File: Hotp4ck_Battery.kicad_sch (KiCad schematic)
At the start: 23 parts, among them J3 Conn_01x02_MountingPin, Q1 2N7002, SW43 PWR, U2 BQ24075, U3 MAX17048

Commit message: Fixed position & etc..
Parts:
- LED2: value orange -> Yellow; footprint LED_SMD:LED_0402_1005Metric -> LED_SMD:LED_0603_1608Metric
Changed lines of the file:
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@@
       (effects (font (size 1.27 1.27)) (justify right))
     )
-    (property "Value" "orange" (at 86.36 71.12 90)
+    (property "Value" "Yellow" (at 86.36 71.12 90)
       (effects (font (size 1.27 1.27)) (justify right))
     )
-    (property "Footprint" "LED_SMD:LED_0402_1005Metric" (at 93.98 74.93 90)
+    (property "Footprint" "LED_SMD:LED_0603_1608Metric" (at 93.98 74.93 90)
       (effects (font (size 1.27 1.27)) hide)
     )

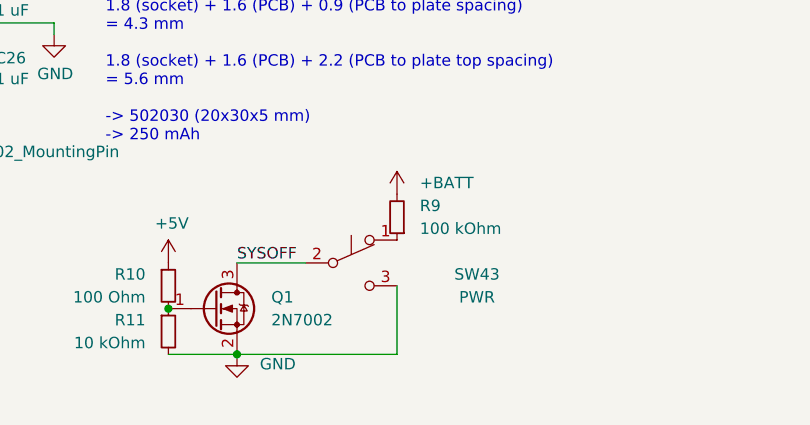
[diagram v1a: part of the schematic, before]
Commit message: Add Switch Mount pin symbol
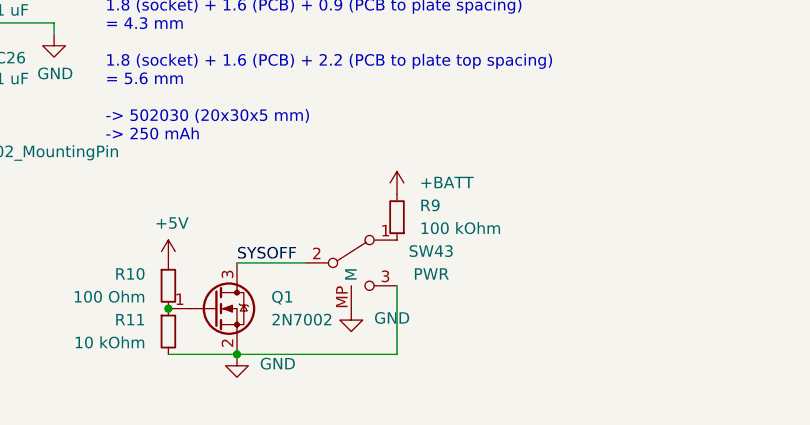
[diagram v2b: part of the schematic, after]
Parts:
- SW43: symbol Switch:SW_Push_SPDT -> marbastlib-various:SW_SPDT_mountpin
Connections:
- net GND: now also SW43.MP (M)
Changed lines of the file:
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@@
     )
   )
-  (symbol (lib_id "Switch:SW_Push_SPDT") (at 157.48 104.14 0) (unit 1)
-    (in_bom yes) (on_board yes) (dnp no)
-    (property "Reference" "SW43" (at 171.45 105.41 0)
-      (effects (font (size 1.27 1.27)))
-    )
-    (property "Value" "PWR" (at 171.45 107.95 0)
-      (effects (font (size 1.27 1.27)))
-    )
-    (property "Footprint" "marbastlib-various:SW_MSK12C02-HB" (at 157.48 104.14 0)
-      (effects (font (size 1.27 1.27)) hide)
-    )
-    (property "Datasheet" "~" (at 157.48 104.14 0)
+  (symbol (lib_id "marbastlib-various:SW_SPDT_mountpin") (at 158.75 104.14 0) (unit 1)
+    (in_bom yes) (on_board yes) (dnp no)
+    (property "Reference" "SW43" (at 166.37 102.87 0)
+      (effects (font (size 1.27 1.27)))
+    )
+    (property "Value" "PWR" (at 166.37 105.41 0)
+      (effects (font (size 1.27 1.27)))
+    )
+    (property "Footprint" "marbastlib-various:SW_MSK12C02-HB" (at 158.75 104.14 0)
+      (effects (font (size 1.27 1.27)) hide)
+    )
+    (property "Datasheet" "~" (at 158.75 104.14 0)
       (effects (font (size 1.27 1.27)) hide)
     )
@@
     (pin "2")
     (pin "3")
+    (pin "MP")
     (instances
       (project "osprey_rev_a"
@@
         )
       )
+    )
+  )
+  (symbol (lib_id "power:GND") (at 157.48 109.22 0) (unit 1)
+    (in_bom yes) (on_board yes) (dnp no) (fields_autoplaced)
+    (property "Reference" "#PWR027" (at 157.48 115.57 0)
+      (effects (font (size 1.27 1.27)) hide)
+    )
+    (property "Value" "GND" (at 160.02 110.2994 0)
+      (effects (font (size 1.27 1.27)) (justify left))
+    )
+    (property "Footprint" "" (at 157.48 109.22 0)
+      (effects (font (size 1.27 1.27)) hide)
+    )
+    (property "Datasheet" "" (at 157.48 109.22 0)
+      (effects (font (size 1.27 1.27)) hide)
+    )
+    (pin "1")
+    (instances
+      (project "osprey_rev_a"
+        (path "/86a516b3-939b-48ee-9a25-d0111c577d06/e12a0b82-f794-4b5e-b657-628292a2530a"
+          (reference "#PWR027") (unit 1)
+        )
+      )
+      (project "Hotp4ck60"
+        (path "/a57939d7-40ce-4436-8014-db245ef7f3c5"
+          (reference "#PWR023") (unit 1)
+        )
+        (path "/a57939d7-40ce-4436-8014-db245ef7f3c5/18c06ada-111b-4ec0-9dc0-78c3052676b0"
+          (reference "#PWR031") (unit 1)
+        )
+      )
+      (project "designguide-schematic"
+        (path "/c2a65ddb-3915-4293-98a9-444287fe2a3d"
+          (reference "#PWR023") (unit 1)
+        )
+      )

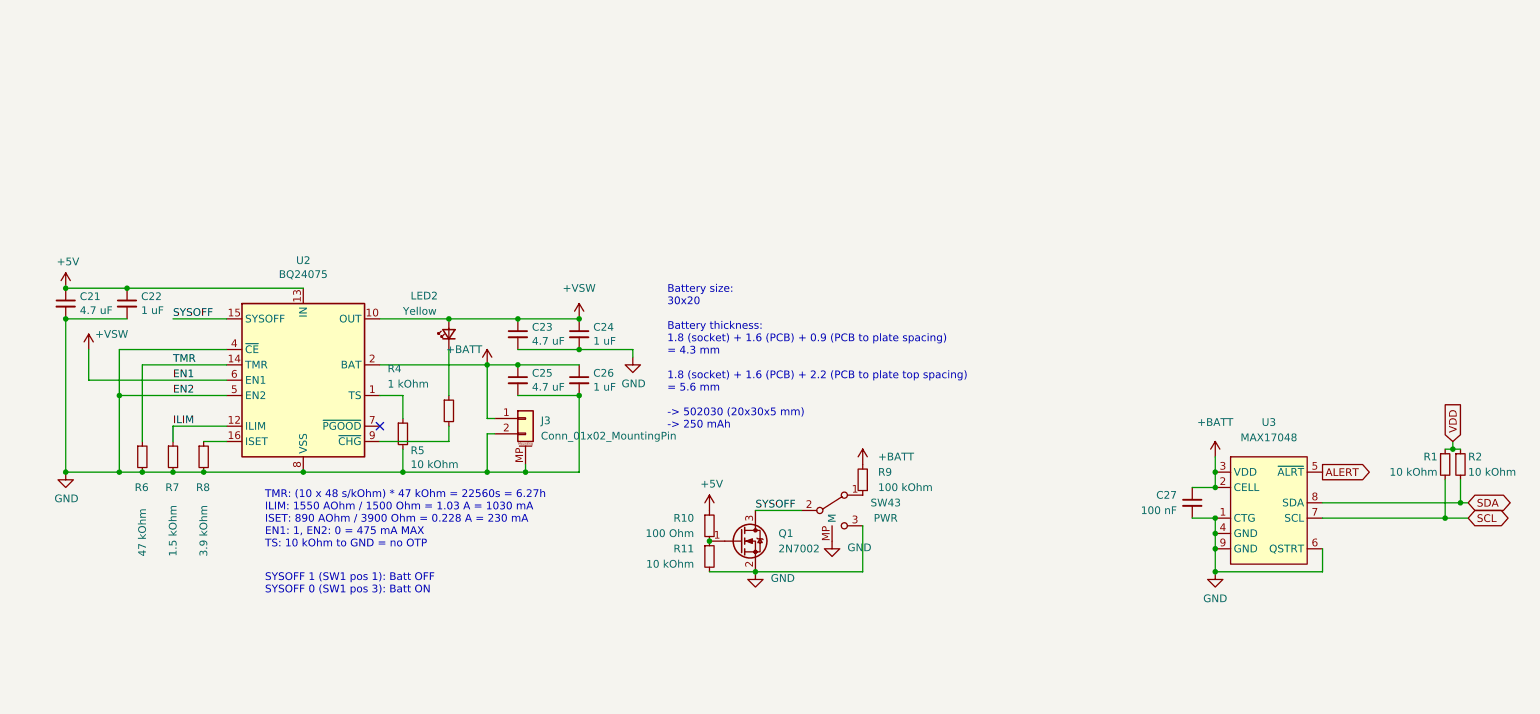
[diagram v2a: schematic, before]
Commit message: update schematic
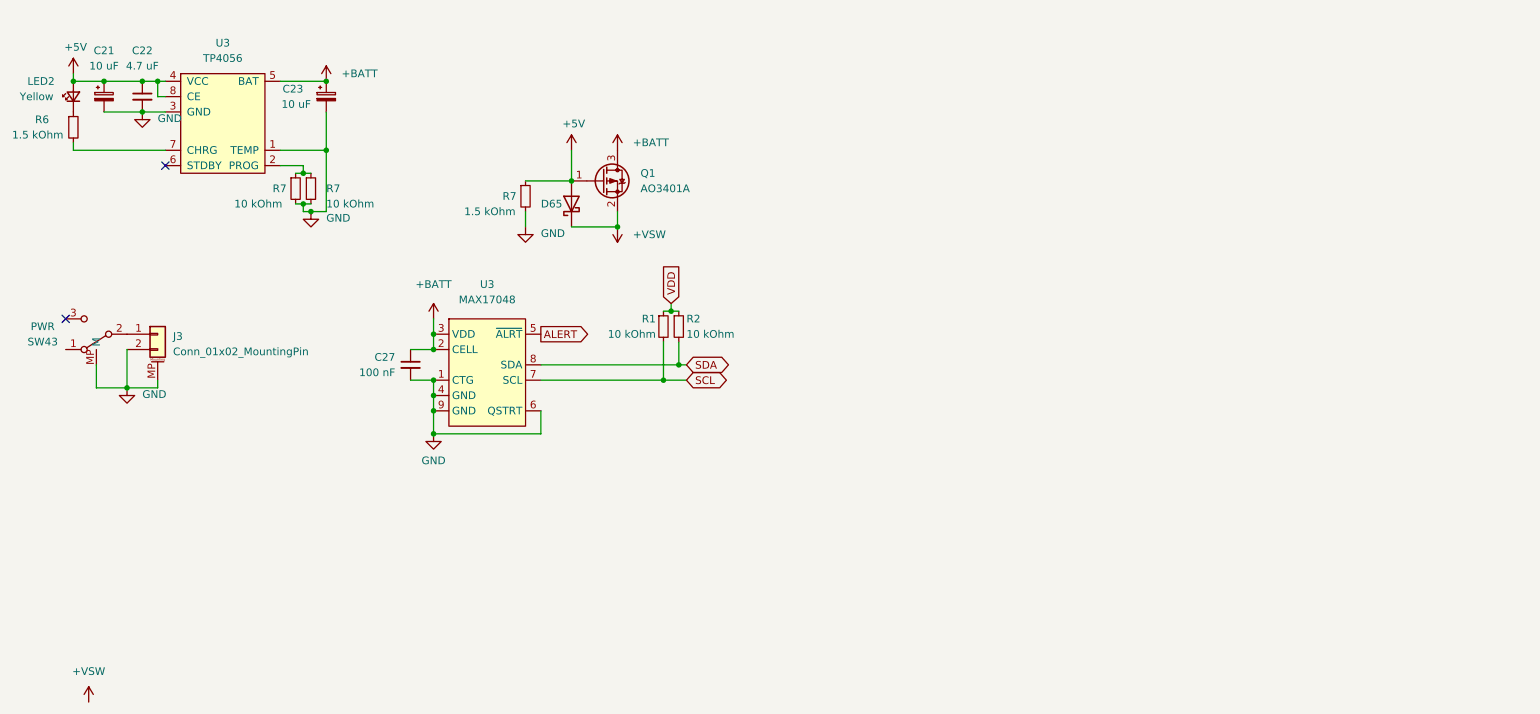
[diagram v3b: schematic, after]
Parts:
- removed C21, C23, C25: 4.7 uF, Capacitor_SMD:C_0402_1005Metric, symbol Device:C_Small
- removed C24, C26: 1 uF, Capacitor_SMD:C_0402_1005Metric, symbol Device:C_Small
- removed Q1: 2N7002, Package_TO_SOT_SMD:SOT-23, symbol Transistor_FET:2N7002
- removed R10: 100 Ohm, Resistor_SMD:R_0402_1005Metric, symbol Device:R_Small
- removed R11, R5: 10 kOhm, Resistor_SMD:R_0402_1005Metric, symbol Device:R_Small
- removed R4: 1 kOhm, Resistor_SMD:R_0402_1005Metric, symbol Device:R_Small
- removed R8: 3.9 kOhm, Resistor_SMD:R_0402_1005Metric, symbol Device:R_Small
- removed R9: 100 kOhm, Resistor_SMD:R_0402_1005Metric, symbol Device:R_Small
- removed U2: BQ24075, Package_DFN_QFN:VQFN-16-1EP_3x3mm_P0.5mm_EP1.6x1.6mm, symbol Battery_Management:BQ24075RGT
- added C21, C23: 10 uF, Capacitor_SMD:C_0805_2012Metric, symbol Device:C_Polarized_Small
- added D65: D_Schottky, Diode_SMD:D_SOD-123, symbol Device:D_Schottky
- added Q1: AO3401A, Package_TO_SOT_SMD:SOT-23, symbol Transistor_FET:AO3401A
- added R7: 1.5 kOhm, Resistor_SMD:R_0402_1005Metric, symbol Device:R_Small
- added R7: 10 kOhm, Resistor_SMD:R_0402_1005Metric, symbol Device:R_Small
- added U3: TP4056, Package_SO:SOP-8-1EP_4.57x4.57mm_P1.27mm_EP4.57x4.45mm, symbol marbastlib-various:TP4056
- C22: value 1 uF -> 4.7 uF
- R6: value 47 kOhm -> 1.5 kOhm
- R7: value 1.5 kOhm -> 10 kOhm
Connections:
- net TMR is gone; now on an unnamed net: R6.1
- net +5V: now also LED2.2 (A), C21.1, D65.2 (A), Q1.1 (G), R7.1, U3.4 (VCC), U3.8 (CE)
- net +BATT: now also C23.1, Q1.3 (D), U3.5 (BAT); no longer J3.1 (Pin_1)
- net +VSW: now also D65.1 (K), Q1.2 (S); no longer LED2.2 (A)
- net GND: now also C21.2, C23.2, R7.2, R7.2, U3.1 (TEMP), U3.3 (GND); no longer R6.2, SW43.3
- net ILIM: no longer names the net of R7.1
- net ILIM: now also R7.1, U3.2 (PROG)
- net SYSOFF: no longer names the net of SW43.2
- net SYSOFF: now also J3.1 (Pin_1)
- new net: R6.2, U3.7 (CHRG)
- no-connect marks 1 -> 2
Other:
- note removed: "Battery size: 30x20 Battery thickness: 1.8 (socket) + 1.6 (PCB) + 0.9 (PCB to plate spacing) = 4.3 mm 1.8 (socket) + 1.6 (PCB) + 2.2 (PCB to plate top spacing) = 5.6 mm -> 502030 (20x30x5 mm) -> 250 mAh"
- note removed: "SYSOFF 1 (SW1 pos 1): Batt OFF SYSOFF 0 (SW1 pos 3): Batt ON"
- note removed: "TMR: (10 x 48 s/kOhm) * 47 kOhm = 22560s = 6.27h ILIM: 1550 AOhm / 1500 Ohm = 1.03 A = 1030 mA ISET: 890 AOhm / 3900 Ohm = 0.228 A = 230 mA EN1: 1, EN2: 0 = 475 mA MAX TS: 10 kOhm to GND = no OTP"
- moved on the sheet: C22, C27, LED2, R1, R2, R6, R7, U3

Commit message: Change schematic
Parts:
- removed R7: 10 kOhm, Resistor_SMD:R_0402_1005Metric, symbol Device:R_Small
- added C13: 100 nF, Capacitor_SMD:C_0402_1005Metric, symbol Device:C_Small
- added C14 (x2): 1 uF, Capacitor_SMD:C_0402_1005Metric, symbol Device:C_Small
- added U5: XC6206PxxxMR, Package_TO_SOT_SMD:SOT-23-3, symbol Regulator_Linear:XC6206PxxxMR
- R7: value 10 kOhm -> 1.2 kOhm; LCSC C25867 -> C25862
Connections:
- net +BATT: now also J3.1 (Pin_1), SW43.1; no longer Q1.3 (D)
- net +VSW: now also C14.1, U5.3 (VI)
- net GND: now also C13.2, C14.2, C14.2, U5.1 (GND)
- net VDD: now also C13.1, C14.1, U5.2 (VO)
- net at SW43.2: now also Q1.3 (D); no longer J3.1 (Pin_1)
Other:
- moved on the sheet: D65, Q1, R7

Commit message: Update
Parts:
- removed C13: 100 nF, Capacitor_SMD:C_0402_1005Metric, symbol Device:C_Small
- removed C14 (x2): 1 uF, Capacitor_SMD:C_0402_1005Metric, symbol Device:C_Small
- removed SW43: PWR, marbastlib-various:SW_MSK12C02-HB, symbol marbastlib-various:SW_SPDT_mountpin
- removed U5: XC6206PxxxMR, Package_TO_SOT_SMD:SOT-23-3, symbol Regulator_Linear:XC6206PxxxMR
- added SW2: PWR, marbastlib-various:SW_MSK12C02-HB, symbol Connector_Generic_MountingPin:Conn_01x03_MountingPin
- C21, C23: symbol Device:C_Polarized_Small -> Device:C_Small
- R7: LCSC C25862 -> C25867
- U3: footprint Package_SO:SOP-8-1EP_4.57x4.57mm_P1.27mm_EP4.57x4.45mm -> Package_SO:SOIC-8-1EP_3.9x4.9mm_P1.27mm_EP2.29x3mm
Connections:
- net +BATT: now also SW2.1 (Pin_1)
- net GND: now also U3.9, SW2.MP (MountPin)
- net at Q1.3 (D): now also SW2.2 (Pin_2)
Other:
- moved on the sheet: D65, Q1, R7
